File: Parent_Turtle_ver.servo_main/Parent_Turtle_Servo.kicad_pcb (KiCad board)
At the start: 2 copper layers, 70 x 60 mm, 42 parts, among them P1 CONN_02X15, P10 WRITING, P12 5V_in, P2 CONN_02X15, P3 CAN, P4 CAN, P5 PWM, P6 SERIAL0, P7 SERIAL1, P8 WRITING_IN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

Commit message: complete servo main ver.1.0
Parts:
- moved Q1 2.89 mm to (136.4, 88.3), turned to 270 degrees
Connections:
- Q1 pad 1: GND -> Net-(Q1-Pad1)
- Q1 pad 2: Net-(Q1-Pad2) -> GND
- R8 pad 1: Net-(Q1-Pad2) -> Net-(Q1-Pad1)
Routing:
- net Net-(Q1-Pad1): track 0.00 -> 3.19 mm
- net Net-(Q1-Pad2): track 1.63 -> 0.00 mm

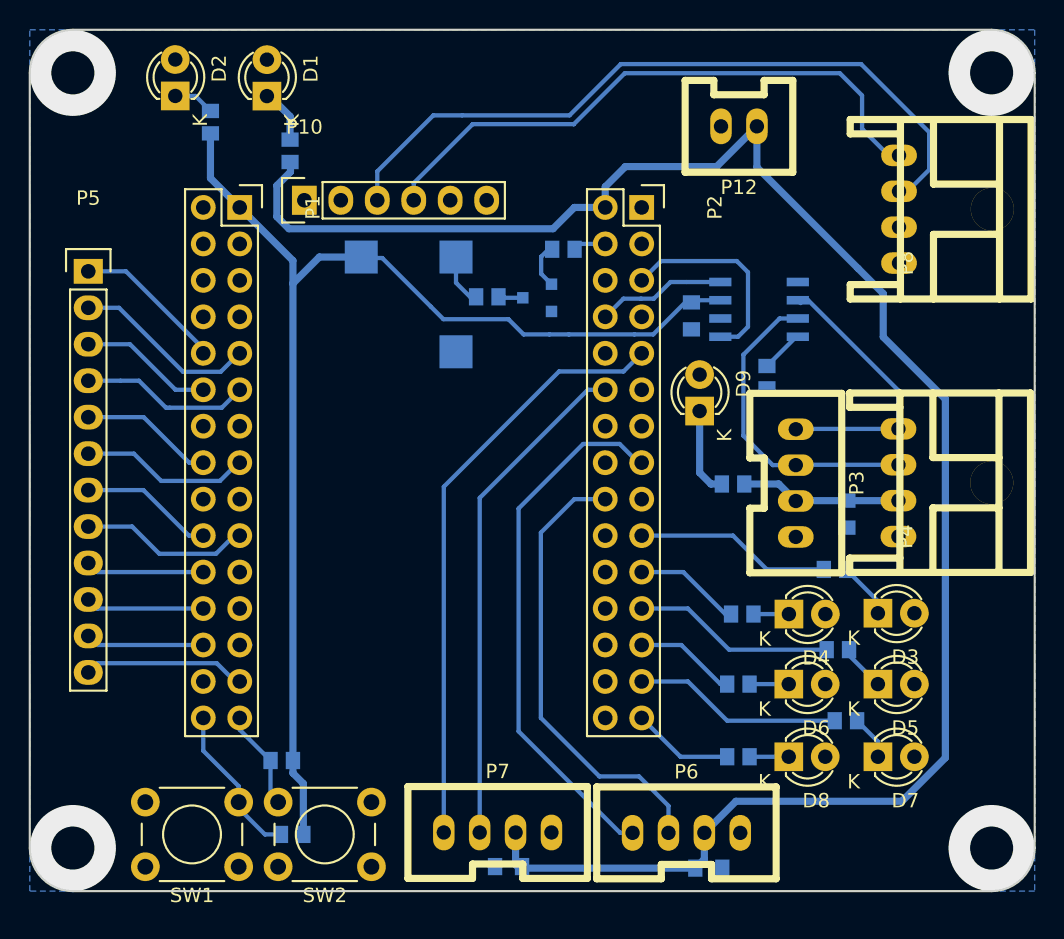
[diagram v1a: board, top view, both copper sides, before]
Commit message: A/Dコンバータのピンの追加
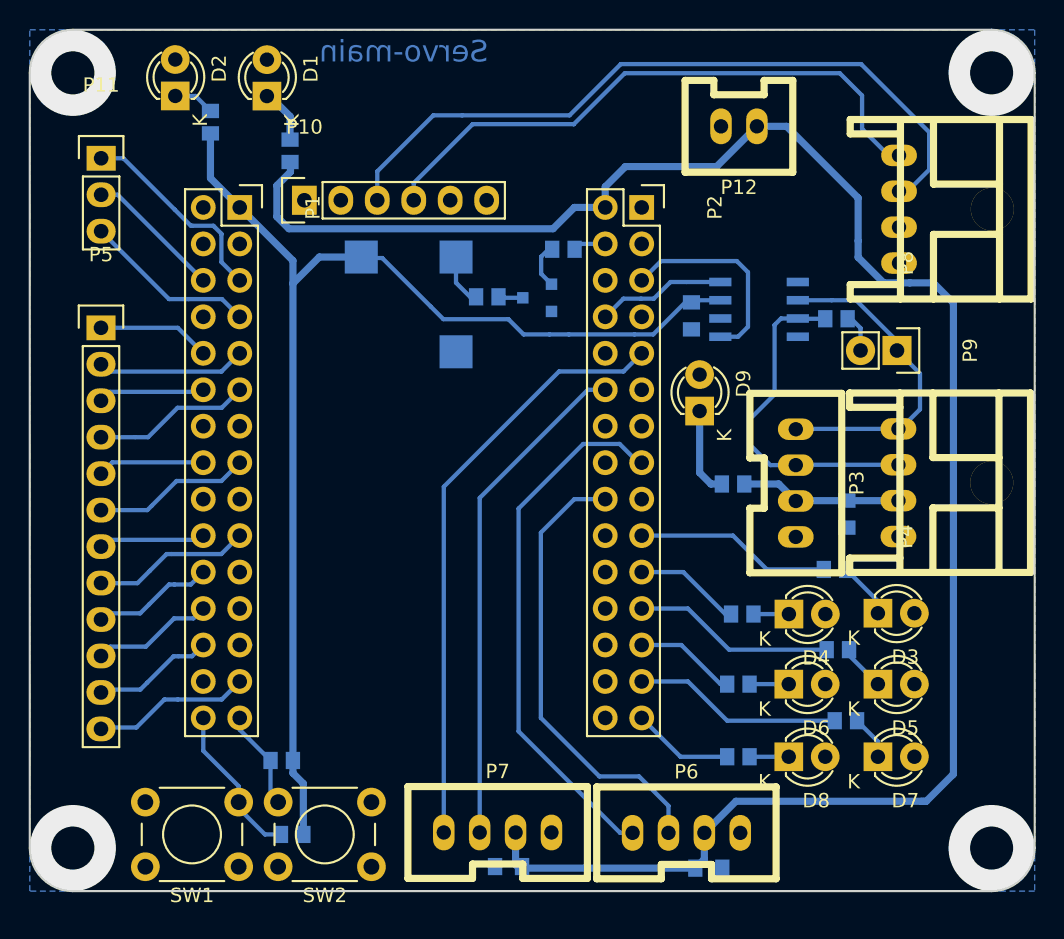
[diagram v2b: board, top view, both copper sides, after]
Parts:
- removed R1: 100k, Resistors_SMD:R_0603
- added P11: A/D, Pin_Headers:Pin_Header_Straight_1x03, F.Cu at (106.1, 78.6)
- added P9: CAN_JP, Pin_Headers:Pin_Header_Straight_1x02, F.Cu at (161.5, 92.0)
- added R15: 120, Resistors_SMD:R_0603, B.Cu at (157.3, 89.8)
- moved P5 4.03 mm to (106.0, 90.4)
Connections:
- U1 pad 5: Net-(U1-Pad5) -> GND
- U1 pad 8: Net-(R1-Pad1) -> GND
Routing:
- net /C0: track 0.00 -> 14.3 mm
- net /C2: track 0.00 -> 12.1 mm
- net /C1: track 0.00 -> 9.59 mm
- net +5V: track 131.0 -> 135.5 mm
- net /CAN_L: track 19.7 -> 22.7 mm
- net Net-(R1-Pad1): track 2.99 -> 0.00 mm
- net Net-(P9-Pad2): track 0.00 -> 2.73 mm
- net /A1: track 10.6 -> 7.86 mm
- net /A0: track 12.9 -> 10.4 mm
- net /CAN_H: track 22.1 -> 24.6 mm
- net /B1: track 9.32 -> 7.44 mm
- net /A3: track 9.32 -> 7.44 mm
- net /A7: track 9.32 -> 7.46 mm
- net /A6: track 11.9 -> 11.0 mm
- net /B0: track 11.9 -> 11.0 mm
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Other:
- board text added: "Servo-main"

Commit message: バージョンを上げた
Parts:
- added P13: CONN_02X04, Pin_Headers:Pin_Header_Straight_2x04, F.Cu at (103.3, 78.8)
- added R1: 100k, Resistors_SMD:R_0603, B.Cu at (156.3, 92.5)
- P11: footprint Pin_Headers:Pin_Header_Straight_1x03 -> Pin_Headers:Pin_Header_Straight_1x04
- moved P11 2.52 mm to (108.6, 78.8)
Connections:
- U1 pad 8: GND -> Net-(R1-Pad1)
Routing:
- net +3.3V: track 85.1 -> 101.7 mm
- net /C3: track 0.00 -> 6.55 mm
- net Net-(R1-Pad1): track 0.00 -> 2.08 mm
- net /C2: track 12.1 -> 10.3 mm
- net /C1: track 9.59 -> 8.27 mm
- net /C0: track 14.3 -> 13.4 mm
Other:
- board text added: "RC19-main"
- board text removed: "Servo-main"
